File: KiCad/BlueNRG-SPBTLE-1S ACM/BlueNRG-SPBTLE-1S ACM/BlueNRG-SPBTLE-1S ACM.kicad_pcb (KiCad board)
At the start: 2 copper layers, 25 x 30.5 mm, 18 parts, among them J1 Conn_01x04_Female, J2 Conn_01x03, U1 LSM6DS3, U2 SPBTLE-1S, U3 TLV70033_SOT23-5

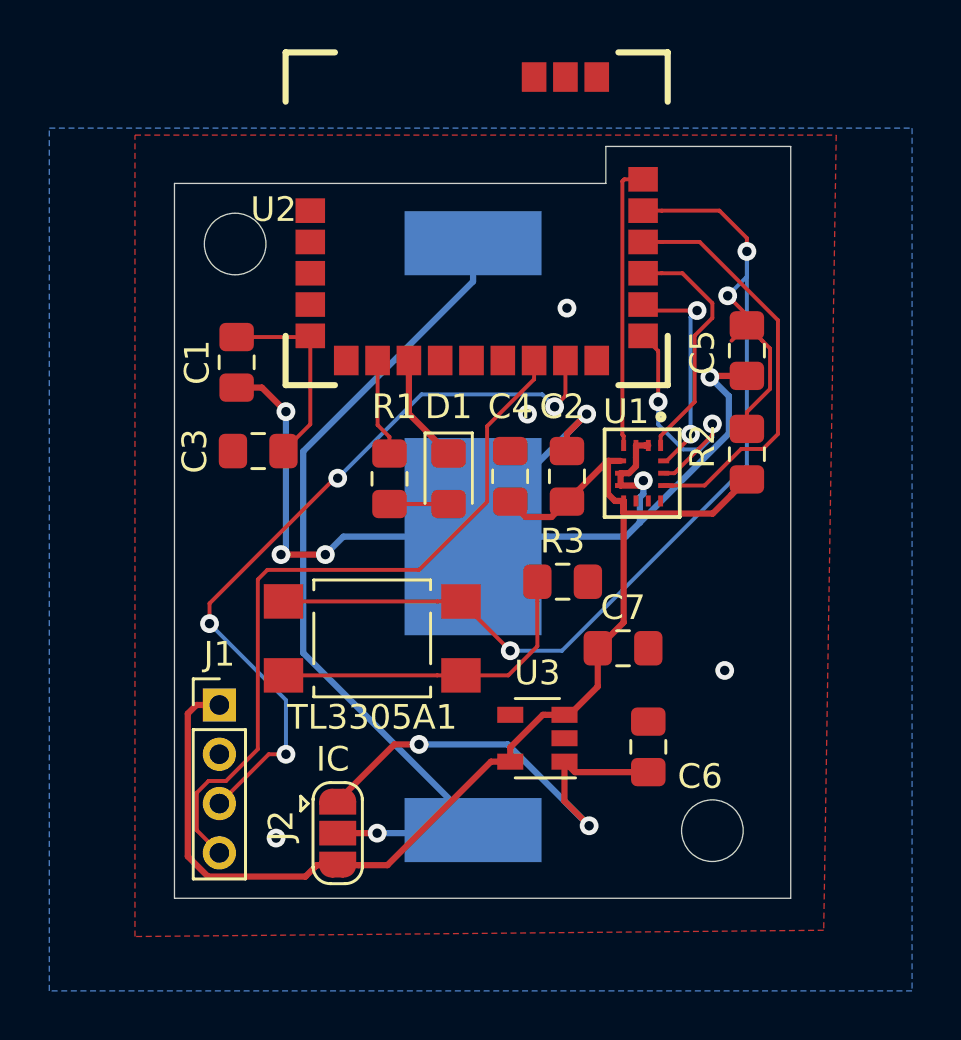
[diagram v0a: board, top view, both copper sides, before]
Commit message: Made the necessary modifications for ACM v2 (circuit logic to Vbat, Vdd to SPTBLE)
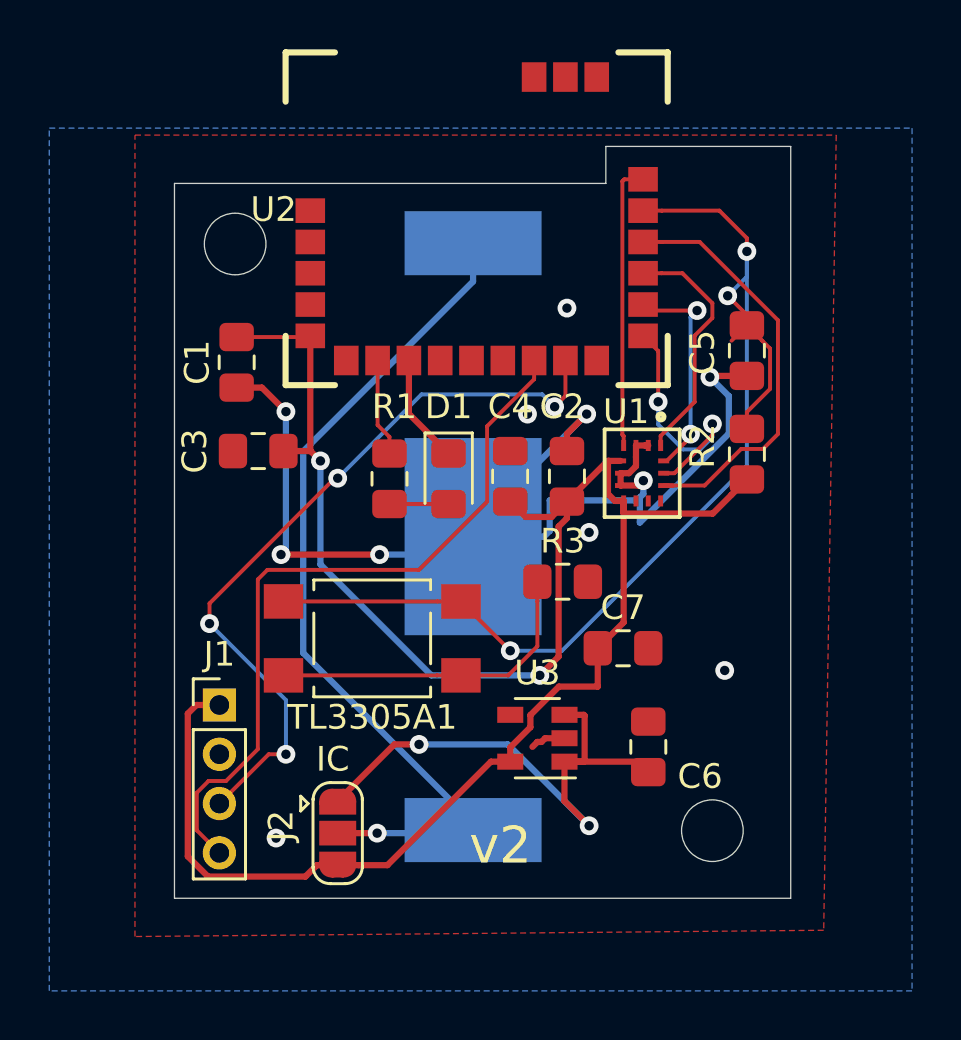
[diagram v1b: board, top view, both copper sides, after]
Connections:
- C1 pad 1: Net-(C1-Pad1) -> Vdd
- C3 pad 1: Net-(C1-Pad1) -> Vdd
- U2 pad 5: Net-(C1-Pad1) -> Vdd
- U3 pad 3: Vdd -> Net-(C6-Pad2)
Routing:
- net Vdd: track 49.5 -> 81.7 mm, vias 0 -> 2
- net Net-(C1-Pad1): track 8.13 -> 0.00 mm
- net Net-(C6-Pad2): track 19.1 -> 22.8 mm
- net GND: track 51.1 -> 53.7 mm, vias 10 -> 11
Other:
- board text added: "v2"

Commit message: Added charging capabilities to ACM PCB and removed the screws. Removed the screws from the cover
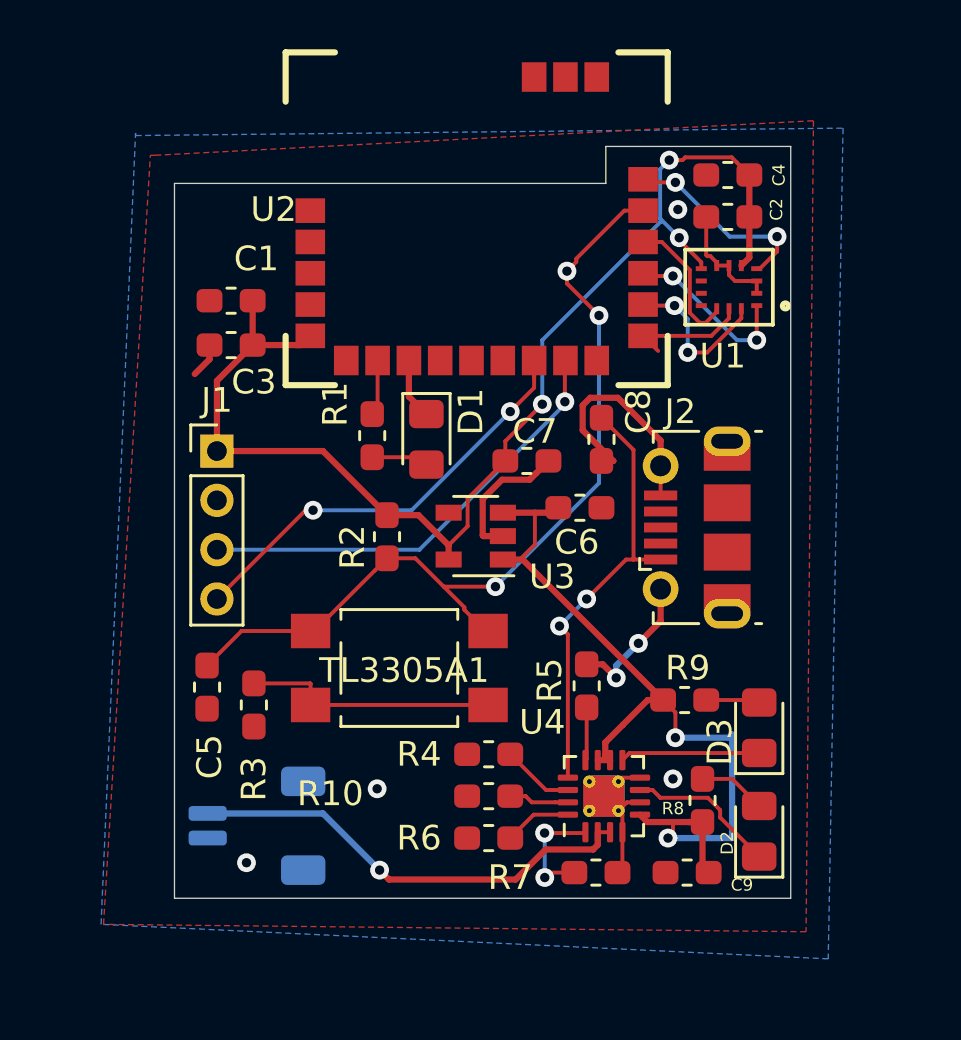
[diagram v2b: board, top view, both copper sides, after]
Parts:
- removed BT1: Battery_Cell, Battery:BatteryHolder_MPD_BC2003_1x2032
- added C8: 1u, Capacitor_SMD:C_0603_1608Metric_Pad1.05x0.95mm_HandSolder, F.Cu at (155.3, 78.4)
- added C9: 4.7u, Capacitor_SMD:C_0603_1608Metric_Pad1.05x0.95mm_HandSolder, F.Cu at (158.8, 96.0)
- added D2: LED, LED_SMD:LED_0805_2012Metric_Pad1.15x1.40mm_HandSolder, F.Cu at (161.7, 94.3)
- added D3: LED, LED_SMD:LED_0805_2012Metric_Pad1.15x1.40mm_HandSolder, F.Cu at (161.7, 90.1)
- added J3: Conn_01x02_Female, Connector_JST:JST_SH_SM02B-SRSS-TB_1x02-1MP_P1.00mm_Horizontal, B.Cu at (141.3, 94.1)
- added R10: 3.57k, Resistor_SMD:R_0603_1608Metric_Pad1.05x0.95mm_HandSolder, F.Cu at (150.7, 92.9)
- added R4: 56.2k, Resistor_SMD:R_0603_1608Metric_Pad1.05x0.95mm_HandSolder, F.Cu at (150.7, 91.2)
- added R5: 2.94k, Resistor_SMD:R_0603_1608Metric_Pad1.05x0.95mm_HandSolder, F.Cu at (154.7, 88.4)
- added R6: 4.32k, Resistor_SMD:R_0603_1608Metric_Pad1.05x0.95mm_HandSolder, F.Cu at (150.7, 94.6)
- added R7: 10k, Resistor_SMD:R_0603_1608Metric_Pad1.05x0.95mm_HandSolder, F.Cu at (155.1, 96.0)
- added R8: 2k, Resistor_SMD:R_0603_1608Metric_Pad1.05x0.95mm_HandSolder, F.Cu at (159.4, 93.0)
- added R9: 2k, Resistor_SMD:R_0603_1608Metric_Pad1.05x0.95mm_HandSolder, F.Cu at (158.7, 89.0)
- added U4: BQ24232, Package_DFN_QFN:VQFN-16-1EP_3x3mm_P0.5mm_EP1.68x1.68mm_ThermalVias, F.Cu at (155.4, 92.9)
- C1, C2, C3, C4, C5, C6, C7: footprint Capacitor_SMD:C_0805_2012Metric_Pad1.15x1.40mm_HandSolder -> Capacitor_SMD:C_0603_1608Metric_Pad1.05x0.95mm_HandSolder
- J2: value Conn_01x03 -> USB_B_Micro; footprint Jumper:SolderJumper-3_P1.3mm_Open_RoundedPad1.0x1.5mm -> Connector_USB:USB_Micro-B_Molex-105017-0001
- R1, R2, R3: footprint Resistor_SMD:R_0805_2012Metric_Pad1.15x1.40mm_HandSolder -> Resistor_SMD:R_0603_1608Metric_Pad1.05x0.95mm_HandSolder
- U2: value SPBTLE-1S -> SPBTLE-1S-Custom_Library
- moved C5 25.8 mm to (139.3, 88.4)
- moved J2 19.1 mm to (159.2, 82.0), turned to 90 degrees
- moved C4 15.1 mm to (160.4, 67.7), turned to 180 degrees
- moved R2 15.0 mm to (146.6, 82.3), turned to 270 degrees
- moved R3 13.5 mm to (141.2, 89.2), turned to 270 degrees
- moved C2 12.4 mm to (160.4, 69.4), turned to 0 degrees
- moved J1 10.3 mm to (139.7, 78.9)
- moved C6 10.1 mm to (154.4, 81.2), turned to 180 degrees
- moved U3 8.57 mm to (150.2, 82.3)
- moved C7 8.54 mm to (152.3, 79.3)
- moved U1 8.33 mm to (160.5, 72.2), turned to 180 degrees
- moved C3 4.44 mm to (140.3, 74.6)
- moved C1 2.51 mm to (140.3, 72.8), turned to 180 degrees
- moved R1 1.88 mm to (146.0, 78.2)
- moved D1 1.84 mm to (148.2, 78.4)
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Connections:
- C6 pad 2: Net-(C6-Pad2) -> VOUT_BQ
- J2 pad 1: Net-(C6-Pad2) -> Net-(C8-Pad1)
- J2 pad 3: Vdd -> Net-(J2-Pad3)
- U3 pad 1: Net-(C6-Pad2) -> VOUT_BQ
- U3 pad 3: Net-(C6-Pad2) -> VOUT_BQ
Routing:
- net VOUT_BQ: track 0.00 -> 35.4 mm, vias 0 -> 2
- net Net-(J2-Pad2): track 35.1 -> 0.00 mm, vias 1 -> 0
- net Vdd: track 81.7 -> 50.3 mm, vias 2 -> 3
- net Net-(C6-Pad2): track 22.8 -> 0.00 mm, vias 2 -> 0
- net Net-(J3-Pad1): track 0.00 -> 18.5 mm, vias 0 -> 1
- net Net-(C8-Pad1): track 0.00 -> 17.8 mm, vias 0 -> 2
- net GND: track 53.7 -> 36.7 mm, vias 11 -> 6
- net JTMS-SWTDIO: track 30.7 -> 18.3 mm, vias 4 -> 1
- net JTCK-SWCTK: track 30.0 -> 18.3 mm, vias 0 -> 2
- net SPI_CS: track 17.3 -> 5.68 mm
- net Net-(C5-Pad1): track 46.2 -> 35.8 mm
- net Net-(D2-Pad1): track 0.00 -> 6.13 mm
- net Net-(D3-Pad1): track 0.00 -> 5.67 mm
- net SPI_CLK: track 10.3 -> 5.03 mm, vias 2 -> 0
- net Net-(R7-Pad1): track 0.00 -> 4.76 mm, vias 0 -> 2
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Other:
- outline, holes or cut-outs redrawn
- board text removed: "GND"
- board text removed: "IC"
- board text removed: "v2"

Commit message: Modified the charging feature
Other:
- board text added: "v3"
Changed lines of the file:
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@@
-(kicad_pcb (version 20171130) (host pcbnew "(5.0.2)-1")
+(kicad_pcb (version 20171130) (host pcbnew "(5.1.2)-1")
   (general
     (thickness 1.6)
-    (drawings 6)
+    (drawings 7)
     (tracks 254)
     (zones 0)
@@
   )
   (setup
-    (last_trace_width 0.16)
+    (last_trace_width 0.254)
     (user_trace_width 0.16)
     (user_trace_width 0.508)
@@
     (zone_45_only no)
     (trace_min 0.16)
-    (segment_width 0.2)
-    (edge_width 0.2)
     (via_size 0.762)
     (via_drill 0.381)
@@
     (uvia_min_size 0.2)
     (uvia_min_drill 0.1)
+    (edge_width 0.2)
+    (segment_width 0.2)
     (pcb_text_width 0.3)
     (pcb_text_size 1.5 1.5)
@@
     (mod_text_size 1 1)
     (mod_text_width 0.15)
-    (pad_size 1.2 1.8)
+    (pad_size 1.5 1.9)
     (pad_drill 0)
     (pad_to_mask_clearance 0.0508)
@@
     )
   )
+  (gr_text v3 (at 141.6558 87.376) (layer B.SilkS)
+    (effects (font (size 1.524 1.524) (thickness 0.15)) (justify mirror))
+  )
   (gr_line (start 155.5 66.5) (end 155.5 68) (layer Edge.Cuts) (width 0.0254))

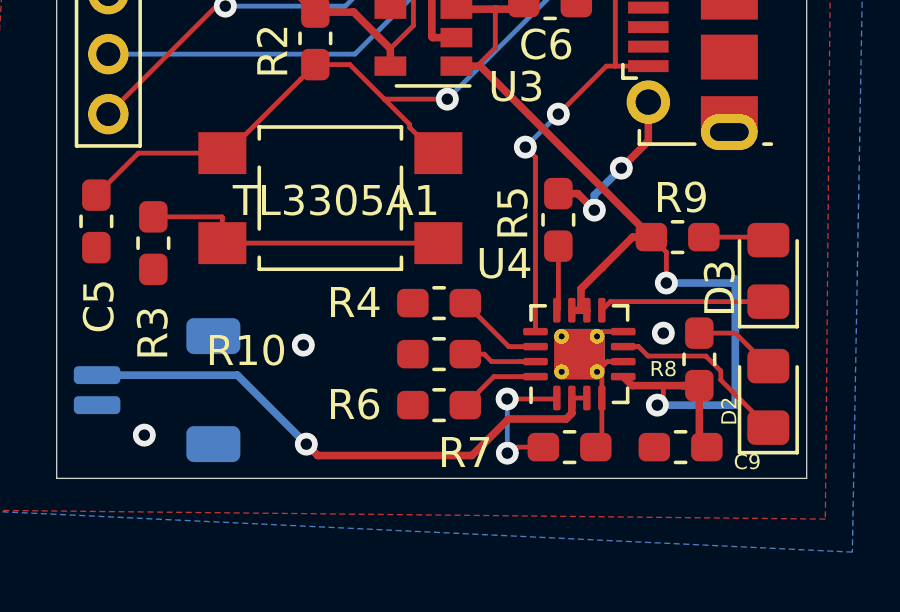
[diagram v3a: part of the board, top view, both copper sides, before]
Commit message: Fixed the PCB layout and schematic for the charger U
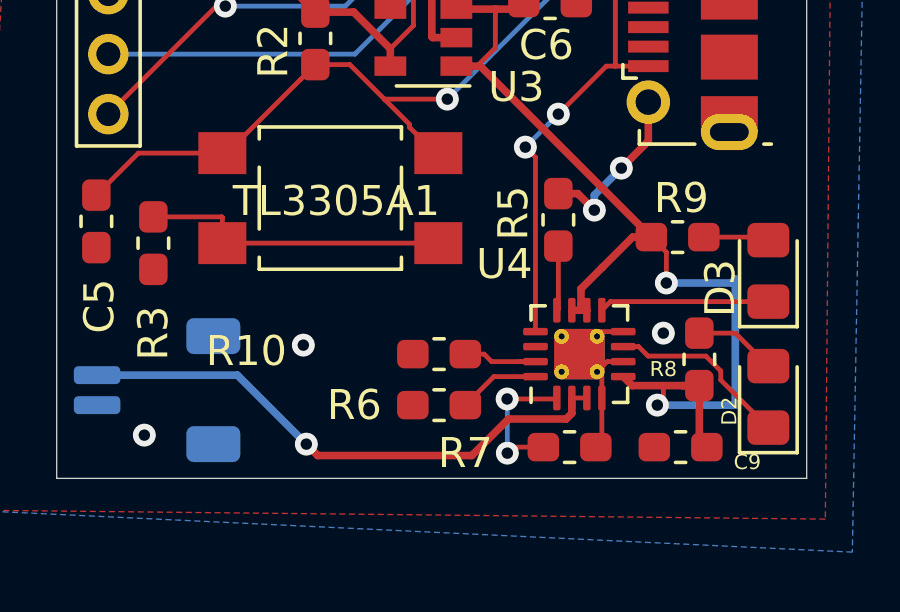
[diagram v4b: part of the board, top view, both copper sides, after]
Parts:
- removed R4: 56.2k, Resistor_SMD:R_0603_1608Metric_Pad1.05x0.95mm_HandSolder
- R10: value 3.57k -> 5.49k
- R5: value 2.94k -> 7.68k
- R6: value 4.32k -> 8.66k
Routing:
- net Net-(U4-Pad14): track 2.94 -> 0.00 mm

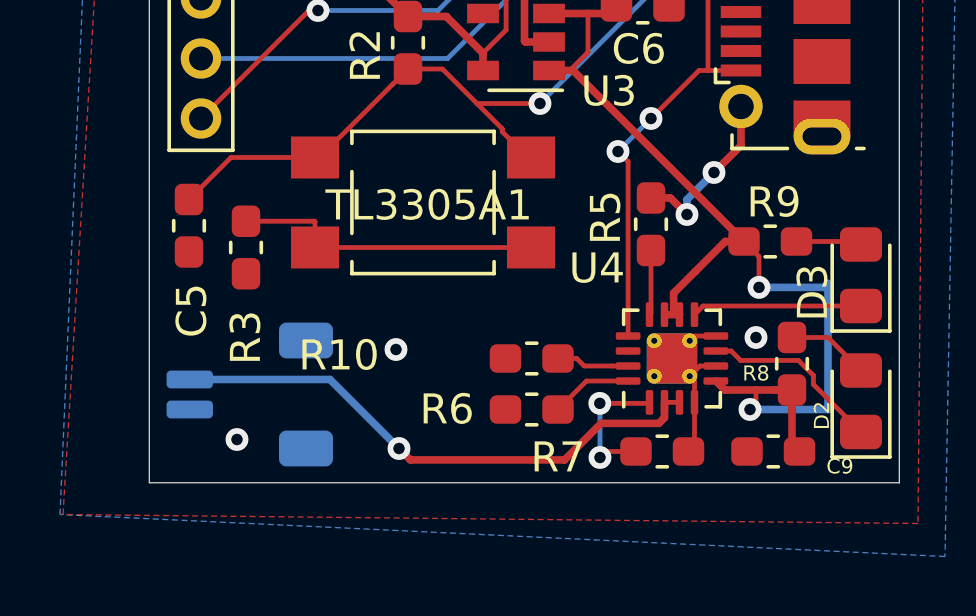
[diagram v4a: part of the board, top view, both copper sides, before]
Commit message: Changed the female connector for the battery. Changed the BQ circuitry
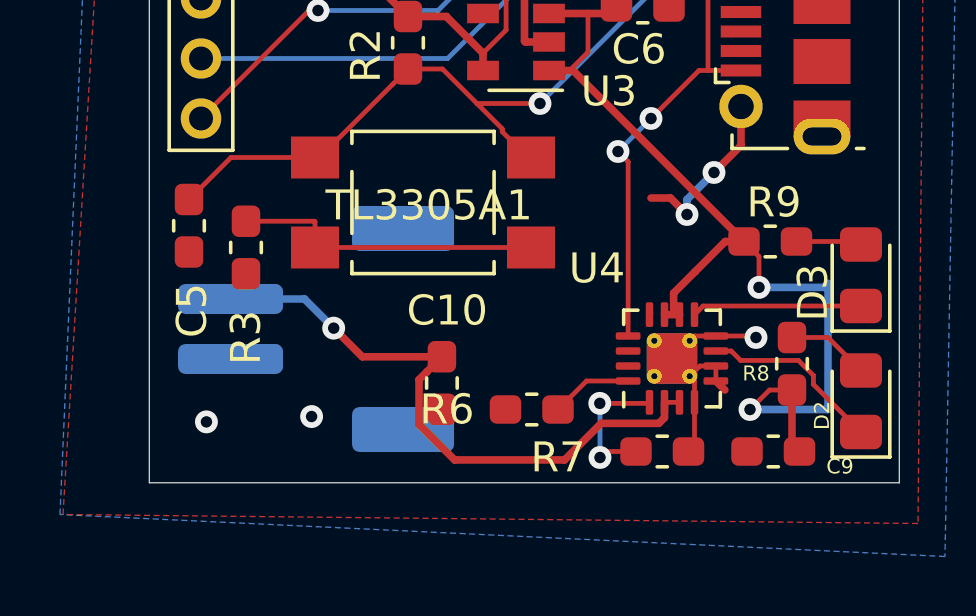
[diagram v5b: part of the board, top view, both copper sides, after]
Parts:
- removed R10: 5.49k, Resistor_SMD:R_0603_1608Metric_Pad1.05x0.95mm_HandSolder
- removed R5: 7.68k, Resistor_SMD:R_0603_1608Metric_Pad1.05x0.95mm_HandSolder
- added C10: 4.7u, Capacitor_SMD:C_0603_1608Metric_Pad1.05x0.95mm_HandSolder, F.Cu at (147.8, 93.7)
- J3: footprint Connector_JST:JST_SH_SM02B-SRSS-TB_1x02-1MP_P1.00mm_Horizontal -> Connector_JST:JST_PH_S2B-PH-SM4-TB_1x02-1MP_P2.00mm_Horizontal
- R6: value 8.66k -> 11.5k
- moved J3 3.11 mm to (143.6, 91.9)
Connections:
- U4 pad 5: VOUT_BQ -> GND
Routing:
- net Net-(U4-Pad15): track 2.44 -> 0.00 mm
- net GND: track 37.1 -> 39.3 mm
- net Net-(C10-Pad2): track 18.5 -> 20.7 mm
- net Net-(U4-Pad12): track 2.16 -> 0.07 mm
- net VOUT_BQ: track 35.4 -> 33.4 mm

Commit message: Few changes before order
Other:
- board text added: "v4"
- board text removed: "v3"
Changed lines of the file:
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@@
-(kicad_pcb (version 20171130) (host pcbnew "(5.1.2)-2")
+(kicad_pcb (version 20171130) (host pcbnew "(5.0.2)-1")
   (general
     (thickness 1.6)
@@
     (zone_45_only no)
     (trace_min 0.16)
+    (segment_width 0.2)
+    (edge_width 0.2)
     (via_size 0.762)
     (via_drill 0.381)
@@
     (uvia_min_size 0.2)
     (uvia_min_drill 0.1)
-    (edge_width 0.2)
-    (segment_width 0.2)
     (pcb_text_width 0.3)
     (pcb_text_size 1.5 1.5)
@@
     (tags "resistor handsolder")
     (attr smd)
-    (fp_text reference R6 (at -2.825 0) (layer F.SilkS)
+    (fp_text reference R6 (at -0.025 -2.1) (layer F.SilkS)
       (effects (font (size 1 1) (thickness 0.15)))
     )
@@
     )
   )
-  (gr_text v3 (at 142.3416 86.0298) (layer B.SilkS)
+  (gr_text v4 (at 142.3416 86.0298) (layer B.SilkS)
     (effects (font (size 1.524 1.524) (thickness 0.15)) (justify mirror))
   )
